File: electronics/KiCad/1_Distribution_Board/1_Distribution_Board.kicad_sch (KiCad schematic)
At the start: 12 parts, among them Q1 DMG2305UX, U1 KH-2.54FH-1X20P-H8.5, U2 KH-2.54FH-1X20P-H8.5

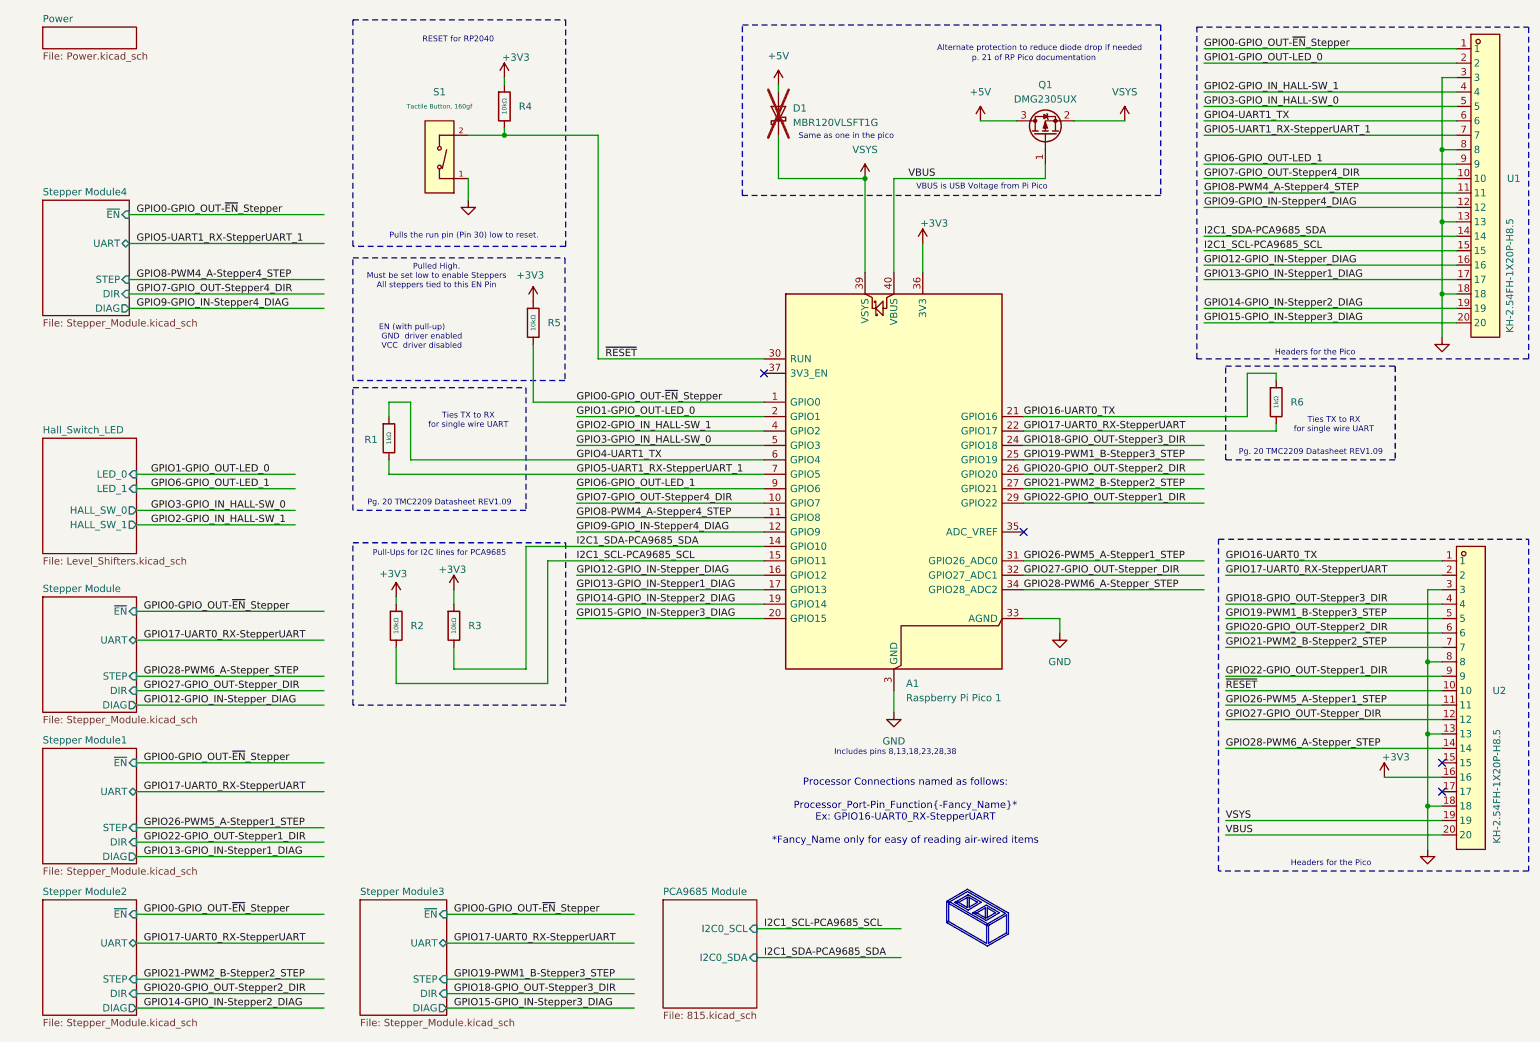
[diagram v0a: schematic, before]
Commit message: distribution board v1.4: hardwired driver addresses, led ports on 24 v, no module headers, fill-only logo, rev in silkscreen
Stepper driver UART addresses are now fixed in copper:
- Removed the ten MS1/MS2 jumper headers (J21, J22, J25, J26, J29, J30,
  J33, J34, J37, J38) and the twenty 10k resistors that served only them
  (R61-R64, R67-R70, R73-R76, R79-R82, R85-R88). The DIAG pull-ups R13,
  R16, R65, R66 and R71 stay, and so does R72, the series resistor of
  the VSYS LED D7.
- Each driver's MS1 (AD0) and MS2 (AD1) pins are tied straight to GND or
  +3V3 through new sheet pins on the root sheet: A2 = 0, A3 = 1, A4 = 2,
  A5 = 3 on UART0 and A6 = 0 on UART1. This is the address map the
  firmware already uses (TMC_UART_ADDRESSES), so firmware does not change.
- On the board the low pins join the ground pour, two of them through a
  short ground stitch and via, and the high pins get short bottom-layer
  +3V3 tracks. Tracks and vias that only served the jumpers are removed.
- Removed the jumper silkscreen: the Pins/Setting legend, the "1 2 3" and
  "3 2 1" pin numbers, the MS1/MS2 labels and "!Double check!".
- The Stepper_Module sheet loses its jumper block and microstep table; a
  note on the root sheet gives the address map.

LED and fan ports run straight from 24 V:
- Removed the 180 ohm resistors R21, R22, R27, R28 and the bypass solder
  jumpers JP1-JP4. Pin 1 of J8, J9, J10 and J11 now connects directly to
  +24V, the state v1.3 boards were built in with the bypasses bridged.
- Removed the four "Bypass Rxx" labels.

Plug-in PCA9685 module headers removed:
- Removed J14, J15, J16, J18, J19 and J20, the module's silkscreen outline,
  the "A10" label and the three tracks that only went to J16. A new ground
  via replaces J16's ground pin as the stitch for that patch of ground pour.
- The on-board PCA9685 (U7) and everything it uses stay, including the
  220 ohm output resistors R43-R58 on the path to J17 and J12.

Oscillator follow-ups:
- D1 (MBR120VLSFT1G, LC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
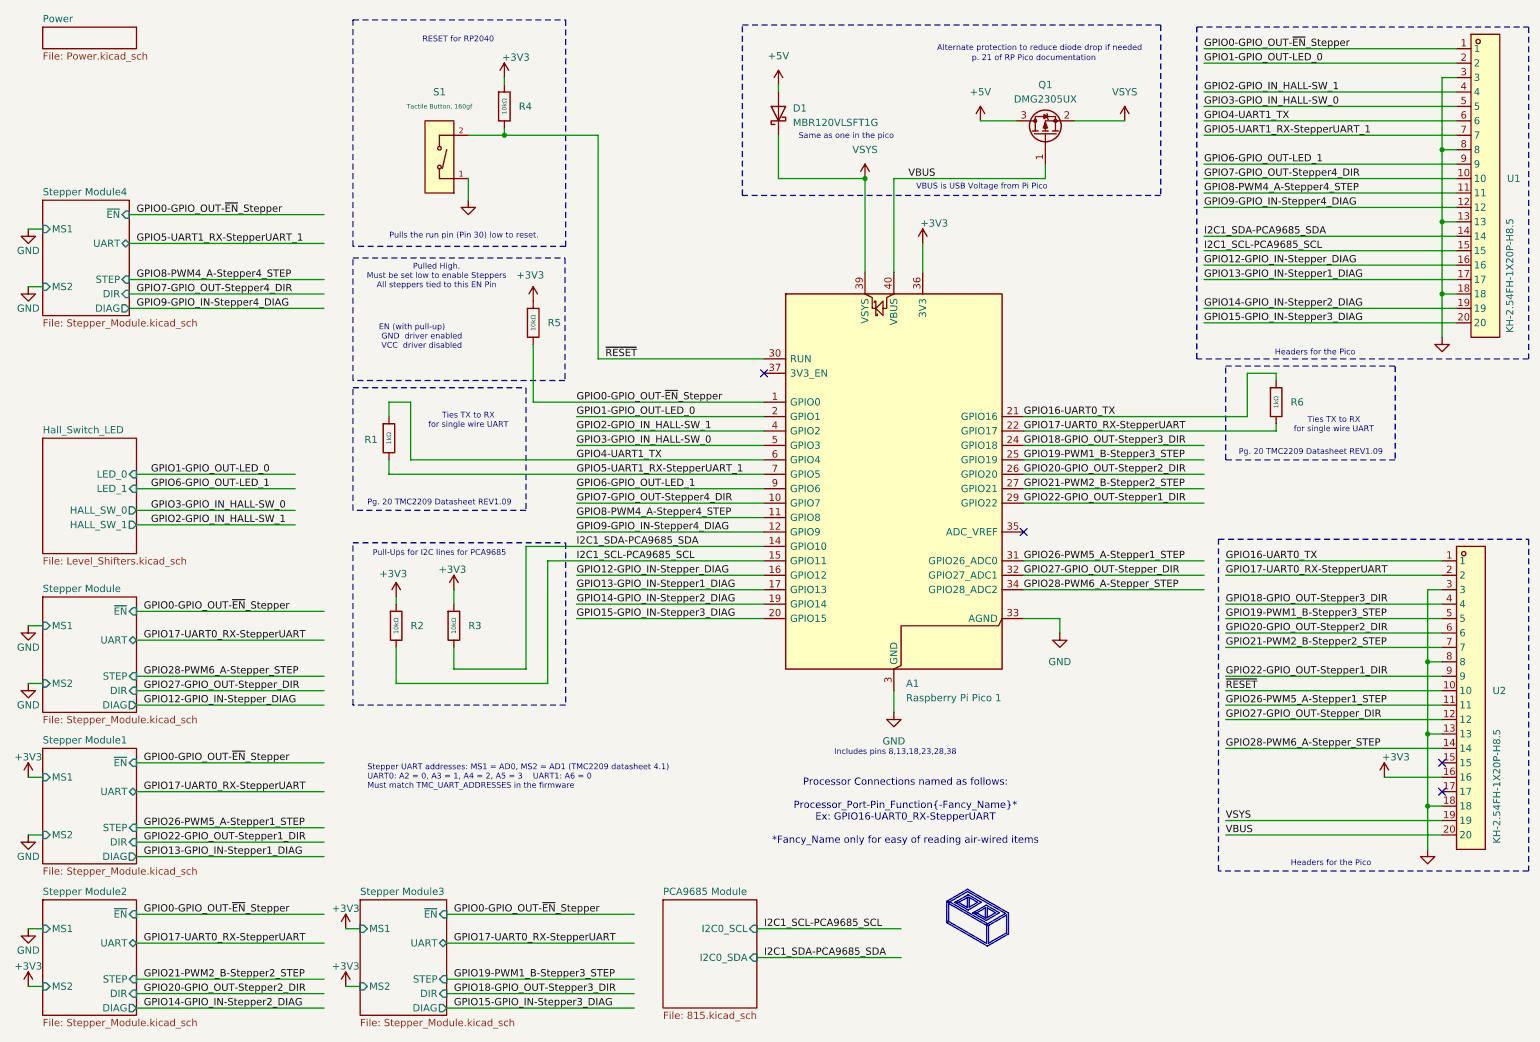
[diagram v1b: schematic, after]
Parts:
- D1: LCSC (none) -> C223608; now fitted
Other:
- sheet Stepper Module ports: added MS1, MS2; removed none
- sheet Stepper Module1 ports: added MS1, MS2; removed none
- sheet Stepper Module2 ports: added MS1, MS2; removed none
- sheet Stepper Module3 ports: added MS1, MS2; removed none
- sheet Stepper Module4 ports: added MS1, MS2; removed none
- note added: "Stepper UART addresses: MS1 = AD0, MS2 = AD1 (TMC2209 datasheet 4.1) UART0: A2 = 0, A3 = 1, A4 = 2, A5 = 3 UART1: A6 = 0 Must match TMC_UART_ADDRESSES in the firmware"

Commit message: distribution board v1.5: serial bus servos on gp2 instead of the second hall input
GP2 read the second hall/switch input (J6, with R12 and C8). It now drives a
half-duplex bus for serial bus servos (Waveshare SC15 / FEETECH SCS15 type,
default 1 Mbps) on pin 1 of CN2 and CN1, the net renamed SERVO_DATA from
WAVESHARE_DATA. One hall/switch input remains (J5, GP3).

- R15 (100 ohm) in series with GP2, then Q6 (BSS138) as a bidirectional level
  shifter: R89 (4.7k) pulls the Pico side up, R90 (1k) pulls the bus up, both
  to 3.3 V, so a servo driving the line to 5 V never reaches the Pico
- D8 (LESD5D5.0CT1G, bidirectional ESD) at CN2 pin 1
- J6, R12, C8 and their silkscreen removed
- REV 1.5 in the silkscreen, the copper text and the title blocks

Firmware needs a half-duplex UART on GP2 (a PIO program with TX and RX on the
one pin). The PCA9685 PWM servo outputs are unchanged.

DRC against v1.4: no new violations, no unconnected items, schematic parity
unchanged.

Co-Authored-By: Claude Opus 5.5 <noreply@anthropic.com>
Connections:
- net GPIO2-GPIO_IN_HALL-SW_1 renamed GPIO2-SERVO_BUS
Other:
- sheet Hall_Switch_LED ports: added SERVO_BUS, SERVO_DATA; removed HALL_SW_1
- sheet Power ports: added SERVO_DATA; removed none
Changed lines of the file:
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@@
 	(title_block
 		(title "Distribution Board")
-		(date "2026-10-14")
-		(rev "1.4")
+		(date "2026-10-18")
+		(rev "1.5")
 		(company "basically")
 	)
@@
 		)
 	)
+	(wire
+		(pts
+			(xy 35.56 105.41) (xy 38.1 105.41)
+		)
+		(stroke
+			(width 0)
+			(type default)
+		)
+	)
+	(label "SERVO_DATA"
+		(at 38.1 105.41 0)
+		(effects
+			(font
+				(size 1.27 1.27)
+			)
+			(justify left bottom)
+		)
+	)
+	(wire
+		(pts
+			(xy 35.56 17.78) (xy 38.1 17.78)
+		)
+		(stroke
+			(width 0)
+			(type default)
+		)
+	)
+	(label "SERVO_DATA"
+		(at 38.1 17.78 0)
+		(effects
+			(font
+				(size 1.27 1.27)
+			)
+			(justify left bottom)
+		)
+	)
 	(label "GPIO20-GPIO_OUT-Stepper2_DIR"
 		(at 36.83 185.42 0)
@@
 		)
 	)
-	(label "GPIO2-GPIO_IN_HALL-SW_1"
+	(label "GPIO2-SERVO_BUS"
 		(at 113.03 86.36 0)
 		(effects
@@
 		)
 	)
-	(label "GPIO2-GPIO_IN_HALL-SW_1"
+	(label "GPIO2-SERVO_BUS"
 		(at 223.52 26.67 0)
 		(effects
@@
 		)
 	)
-	(label "GPIO2-GPIO_IN_HALL-SW_1"
+	(label "GPIO2-SERVO_BUS"
 		(at 38.1 102.87 0)
 		(effects
@@
 			)
 		)
+		(pin "SERVO_DATA" bidirectional
+			(at 35.56 17.78 0)
+			(effects
+				(font
+					(size 1.27 1.27)
+				)
+				(justify right)
+			)
+		)
 		(instances
 			(project "1_Distribution_Board"
@@
 			)
 		)
-		(pin "HALL_SW_1" output
+		(pin "SERVO_BUS" bidirectional
 			(at 35.56 102.87 0)
 			(effects
 				(font
+					(size 1.27 1.27)
+				)
+				(justify right)
+			)
+		)
+		(pin "SERVO_DATA" bidirectional
+			(at 35.56 105.41 0)
+			(effects
+				(font

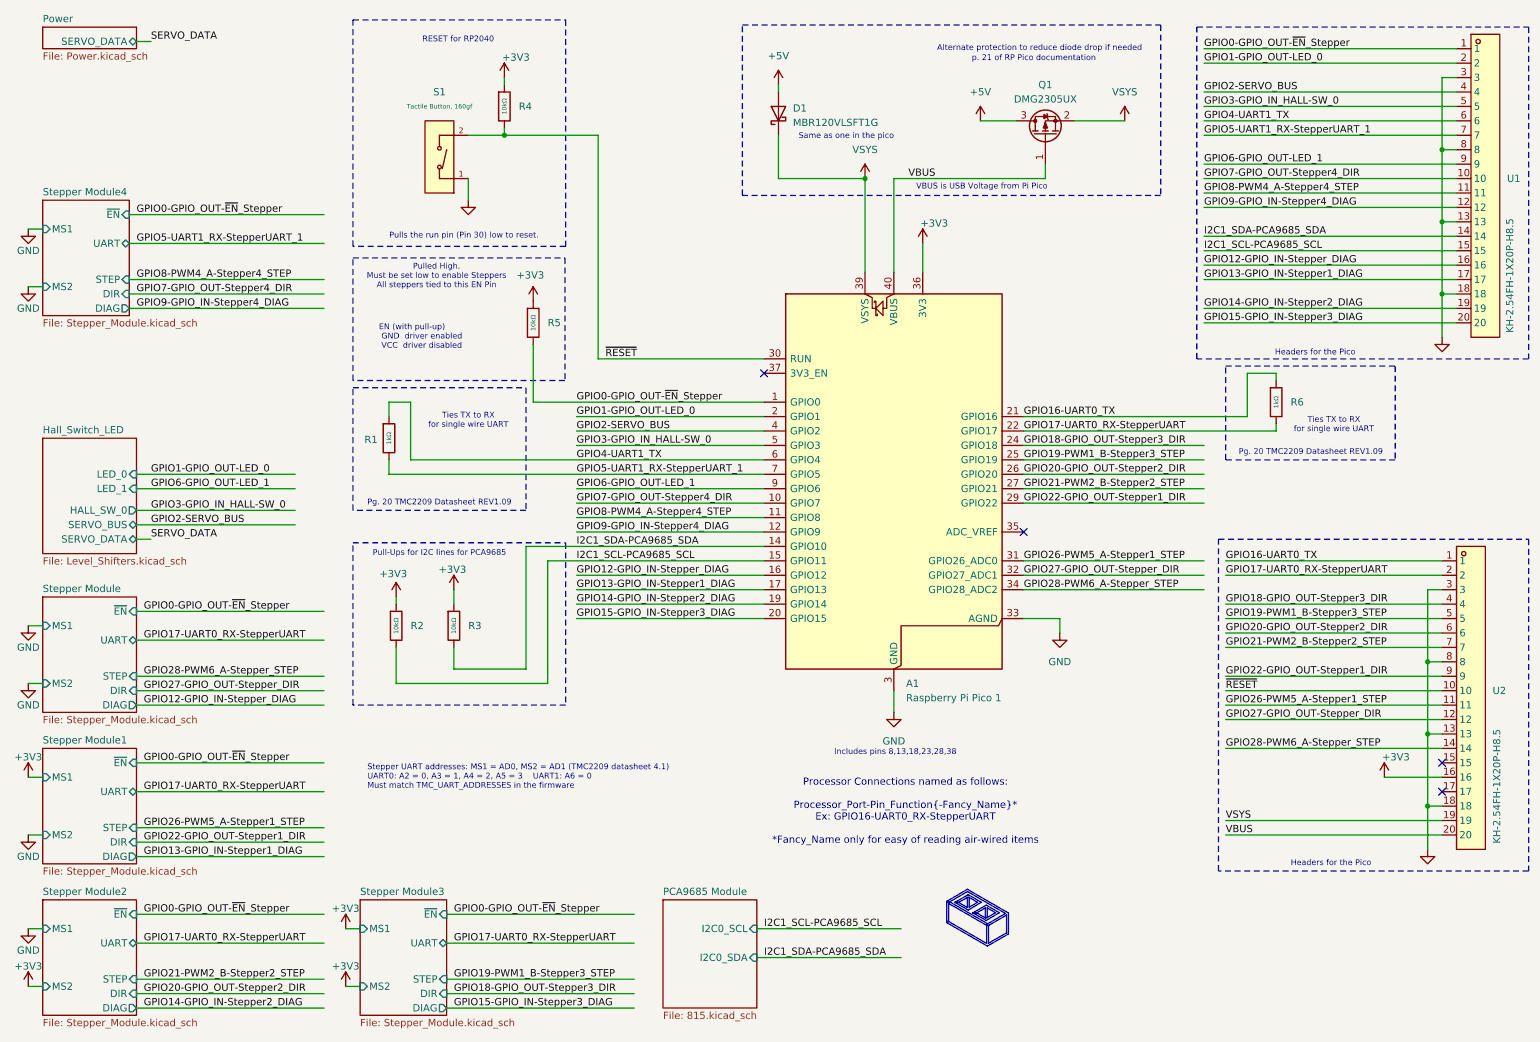
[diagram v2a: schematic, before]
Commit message: distribution board v1.5: drop the pca9685 pwm servo side
The serial-servo revision has no use for the PWM servo path, so it goes:

- the PCA9685 Module sheet: U7 (PCA9685), U6 (PCA9306 I2C level shifter),
  Y1, their capacitors and pull-ups, the A0-A5 address resistors, the 16
  output resistors and the J12, J13 and J17 PWM headers
- R2 and R3, the I2C pull-ups that served only it; GP10 and GP11 are now
  unused, marked no-connect like the other unused Pico pins
- the PWM, address-table and I2C silkscreen, and the pour keepout under J17

Where a removed pad joined two tracks of a net that stays (VSYS, +3V3), the
tracks are joined directly; copper that only led to removed parts is gone.

DRC against the previous commit: no new violations, no unconnected items,
schematic parity unchanged.

Co-Authored-By: Claude Opus 5.5 <noreply@anthropic.com>
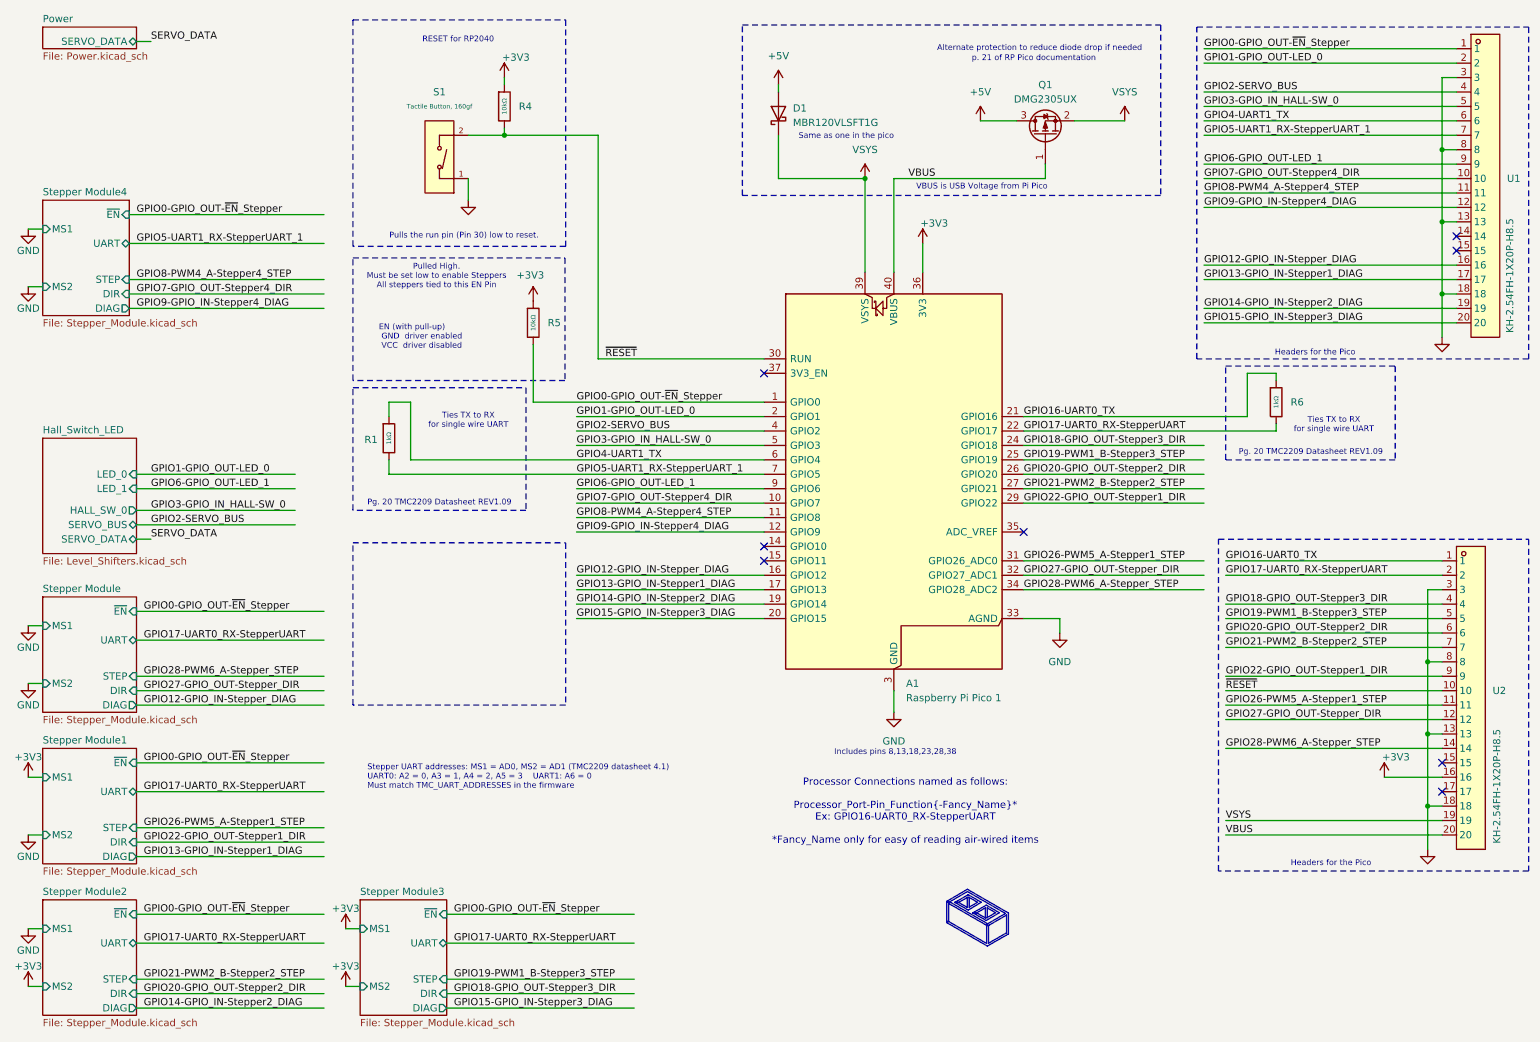
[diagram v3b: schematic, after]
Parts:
- removed R2, R3: 10kΩ, PCM_JLCPCB:R_0603, symbol PCM_JLCPCB-Resistors:0603,10kΩ
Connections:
- net I2C1_SCL-PCA9685_SCL: no longer names the net of U1.15
- net I2C1_SCL-PCA9685_SCL: no longer A1.15 (GPIO11)
- net I2C1_SDA-PCA9685_SDA: no longer names the net of U1.14
- net I2C1_SDA-PCA9685_SDA: no longer A1.14 (GPIO10)
- no-connect marks 4 -> 8
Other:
- removed sheet PCA9685 Module
- note removed: "Pull-Ups for I2C lines for PCA9685"
